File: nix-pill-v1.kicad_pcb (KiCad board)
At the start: 2 copper layers, 75 x 35 mm, 40 parts, among them J1 LEFT, J2 BOOT, J3 RIGHT, J4 SWD, J5 USB_B_Micro, SW1 USER0, SW2 NRST, U1 AMS1117-3.3, U2 STM32F103C8Tx, Y1 32.768KHz LSE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

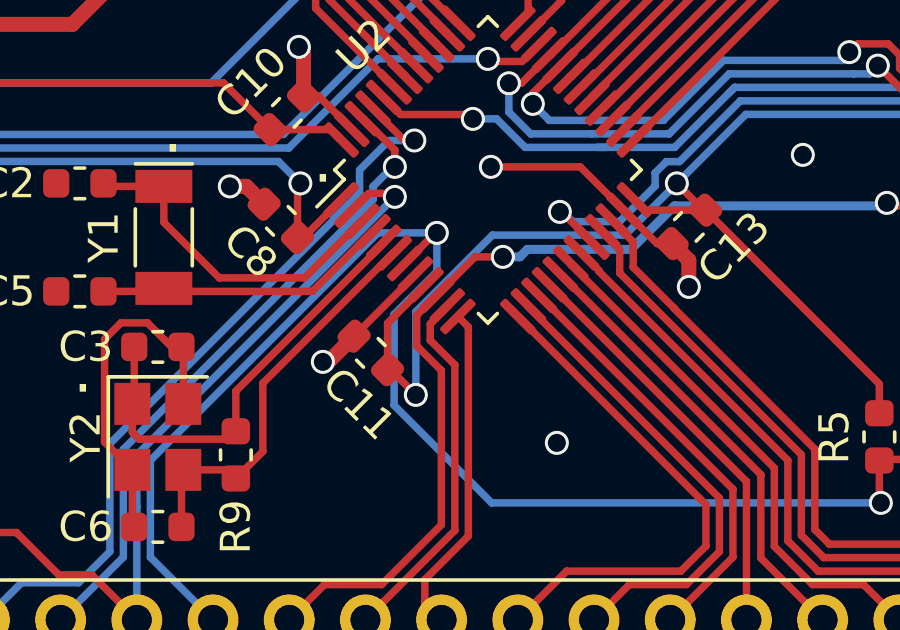
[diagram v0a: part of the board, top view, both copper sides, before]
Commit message: Started adding data sheets Started the BOM Calculated the LED limiting R
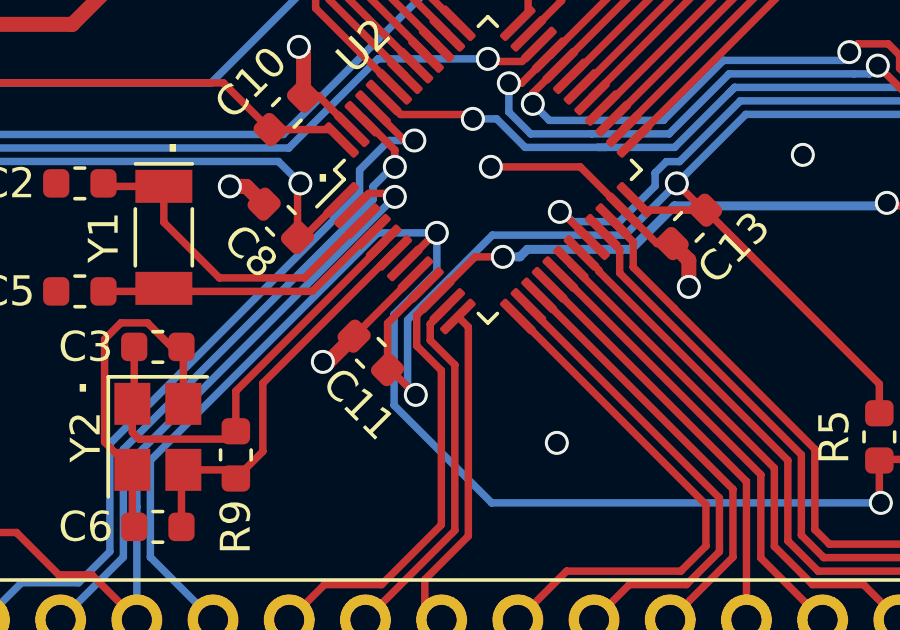
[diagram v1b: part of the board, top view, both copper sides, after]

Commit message: BOM completed. Ordering PCB and parts
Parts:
- C2, C5: value 20pF -> 8pF
- C3, C6: value 20pF -> 10pF
- R1, R2: value 510 -> 100
- R9: value 10M -> 1M
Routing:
- net +3V3: track 214.8 -> 219.5 mm
- net SWDCLK: track 34.5 -> 37.6 mm
- net GND: vias 14 -> 16
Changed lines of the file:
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@@
     (thickness 1.6)
     (drawings 50)
-    (tracks 514)
+    (tracks 522)
     (zones 0)
     (modules 40)
@@
   (page A4)
   (layers
-    (0 F.Cu signal hide)
+    (0 F.Cu signal)
     (31 B.Cu signal)
     (32 B.Adhes user)
@@
       (effects (font (size 1 1) (thickness 0.15)))
     )
-    (fp_text value 20pF (at 0 1.43) (layer F.Fab)
+    (fp_text value 8pF (at 0 1.43) (layer F.Fab)
       (effects (font (size 1 1) (thickness 0.15)))
     )
@@
       (effects (font (size 1 1) (thickness 0.15)))
     )
-    (fp_text value 20pF (at 0 1.43) (layer F.Fab)
+    (fp_text value 10pF (at 0 1.43) (layer F.Fab)
       (effects (font (size 1 1) (thickness 0.15)))
     )
@@
       (effects (font (size 1 1) (thickness 0.15)))
     )
-    (fp_text value 20pF (at 0 1.43) (layer F.Fab)
+    (fp_text value 8pF (at 0 1.43) (layer F.Fab)
       (effects (font (size 1 1) (thickness 0.15)))
     )
@@
       (effects (font (size 1 1) (thickness 0.15)))
     )
-    (fp_text value 20pF (at 0 1.43) (layer F.Fab)
+    (fp_text value 10pF (at 0 1.43) (layer F.Fab)
       (effects (font (size 1 1) (thickness 0.15)))
     )
@@
       (effects (font (size 1 1) (thickness 0.15)))
     )
-    (fp_text value 510 (at 0 1.43 90) (layer F.Fab)
+    (fp_text value 100 (at 0 1.43 90) (layer F.Fab)
       (effects (font (size 1 1) (thickness 0.15)))
     )
@@
       (effects (font (size 1 1) (thickness 0.15)))
     )
-    (fp_text value 510 (at 0 1.43) (layer F.Fab)
+    (fp_text value 100 (at 0 1.43) (layer F.Fab)
       (effects (font (size 1 1) (thickness 0.15)))
     )
@@
       (effects (font (size 1 1) (thickness 0.15)))
     )
-    (fp_text value 10M (at 0 1.43 90) (layer F.Fab)
+    (fp_text value 1M (at 0 1.43 90) (layer F.Fab)
       (effects (font (size 1 1) (thickness 0.15)))
     )
@@
   (segment (start 114.3875 114.6) (end 113.9875 115) (width 0.25) (layer F.Cu) (net 1))
   (segment (start 117.8 114.6) (end 114.3875 114.6) (width 0.25) (layer F.Cu) (net 1))
-  (segment (start 119.3 104.06) (end 120.86 102.5) (width 0.25) (layer F.Cu) (net 1))
-  (segment (start 119.3 106.35) (end 119.3 104.06) (width 0.25) (layer F.Cu) (net 1))
   (segment (start 128.686306 114.6) (end 130.243153 116.156847) (width 0.25) (layer F.Cu) (net 1))
   (segment (start 120.8 114.6) (end 128.686306 114.6) (width 0.25) (layer F.Cu) (net 1))
@@
   (segment (start 146.1 115.65) (end 157.7 115.65) (width 0.25) (layer B.Cu) (net 1))
   (segment (start 114.45 129.5) (end 114.4 129.5) (width 0.25) (layer F.Cu) (net 1))
-  (segment (start 114.4 129.5) (end 113.3 128.4) (width 0.25) (layer F.Cu) (net 1))
-  (segment (start 112.964998 128.4) (end 108.764998 124.2) (width 0.25) (layer F.Cu) (net 1))
-  (segment (start 108.764998 124.2) (end 104.9875 124.2) (width 0.25) (layer F.Cu) (net 1))
-  (segment (start 113.3 128.4) (end 112.964998 128.4) (width 0.25) (layer F.Cu) (net 1))
   (segment (start 134.825009 124.725009) (end 135.1 125) (width 0.25) (layer B.Cu) (net 1))
   (segment (start 134.825009 122.501989) (end 134.825009 124.725009) (width 0.25) (layer B.Cu) (net 1))
@@
   (segment (start 143.8 117.95) (end 142.075001 119.674999) (width 0.25) (layer B.Cu) (net 1))
   (segment (start 142.075001 119.674999) (end 137.651999 119.674999) (width 0.25) (layer B.Cu) (net 1))
+  (segment (start 114.45 129.5) (end 114.45 128.25) (width 0.25) (layer F.Cu) (net 1))
+  (segment (start 114.45 128.25) (end 115.5 127.2) (width 0.25) (layer F.Cu) (net 1))
+  (segment (start 115.5 127.2) (end 115.5 120.7) (width 0.25) (layer F.Cu) (net 1))
+  (segment (start 117.8 118.4) (end 117.8 114.6) (width 0.25) (layer F.Cu) (net 1))
+  (segment (start 115.5 120.7) (end 117.8 118.4) (width 0.25) (layer F.Cu) (net 1))
+  (segment (start 119.3 104.06) (end 120.86 102.5) (width 0.5) (layer F.Cu) (net 1))
+  (segment (start 119.3 106.35) (end 119.3 104.06) (width 0.5) (layer F.Cu) (net 1))
   (via (at 131.2 113.4) (size 0.8) (drill 0.6) (layers F.Cu B.Cu) (net 2))
   (via (at 124 105.6) (size 0.8) (drill 0.6) (layers F.Cu B.Cu) (net 2))
@@
   (via (at 117.4 121.2) (size 0.8) (drill 0.6) (layers F.Cu B.Cu) (net 2))
   (via (at 148 117) (size 0.8) (drill 0.6) (layers F.Cu B.Cu) (net 2))
+  (via (at 111 123.2) (size 0.8) (drill 0.6) (layers F.Cu B.Cu) (net 2))
+  (via (at 166 123.2) (size 0.8) (drill 0.6) (layers F.Cu B.Cu) (net 2))
   (segment (start 124.7875 118.05) (end 124.6875 117.95) (width 0.25) (layer F.Cu) (net 3))
   (segment (start 126.7 118.05) (end 124.7875 118.05) (width 0.25) (layer F.Cu) (net 3))
@@
   (segment (start 139.205895 113.319231) (end 138.637947 113.887179) (width 0.25) (layer F.Cu) (net 45))
   (segment (start 138.637947 113.887179) (end 137.587179 113.887179) (width 0.25) (layer F.Cu) (net 45))
-  (segment (start 106.88999 116.77001) (end 104.8 118.86) (width 0.25) (layer B.Cu) (net 45))
-  (segment (start 137.5 113.8) (end 133.83641 113.8) (width 0.25) (layer B.Cu) (net 45))
-  (segment (start 130.866401 116.770009) (end 106.88999 116.77001) (width 0.25) (layer B.Cu) (net 45))
-  (segment (start 133.83641 113.8) (end 130.866401 116.770009) (width 0.25) (layer B.Cu) (net 45))
-  (segment (start 104.8 116.32) (end 130.68 116.32) (width 0.25) (layer B.Cu) (net 46))
+  (segment (start 136.381637 114.918363) (end 137.5 113.8) (width 0.25) (layer B.Cu) (net 45))
+  (segment (start 135.172222 114.918363) (end 136.381637 114.918363) (width 0.25) (layer B.Cu) (net 45))
+  (segment (start 133.320576 116.770009) (end 135.172222 114.918363) (width 0.25) (layer B.Cu) (net 45))
+  (segment (start 106.88999 116.77001) (end 133.320576 116.770009) (width 0.25) (layer B.Cu) (net 45))
+  (segment (start 104.8 118.86) (end 106.88999 116.77001) (width 0.25) (layer B.Cu) (net 45))
   (segment (start 136.501212 112.612124) (end 136.465856 112.612124) (width 0.25) (layer F.Cu) (net 46))
   (via (at 135.621314 111.378686) (size 0.8) (drill 0.6) (layers F.Cu B.Cu) (net 46))
   (segment (start 136.465856 112.612124) (end 135.621314 111.767582) (width 0.25) (layer F.Cu) (net 46))
   (segment (start 135.621314 111.767582) (end 135.621314 111.378686) (width 0.25) (layer F.Cu) (net 46))
-  (segment (start 135.621314 111.378686) (end 130.68 116.32) (width 0.25) (layer B.Cu) (net 46))
+  (segment (start 133.134175 116.32) (end 134.985822 114.468353) (width 0.25) (layer B.Cu) (net 46))
+  (segment (start 104.8 116.32) (end 133.134175 116.32) (width 0.25) (layer B.Cu) (net 46))
+  (segment (start 136.774999 112.532371) (end 135.621314 111.378686) (width 0.25) (layer B.Cu) (net 46))
+  (segment (start 134.985822 114.468353) (end 136.195237 114.468353) (width 0.25) (layer B.Cu) (net 46))
+  (segment (start 136.195237 114.468353) (end 136.774999 113.888591) (width 0.25) (layer B.Cu) (net 46))
+  (segment (start 136.774999 113.888591) (end 136.774999 112.532371) (width 0.25) (layer B.Cu) (net 46))
   (segment (start 167.8125 118.075) (end 170.235 118.075) (width 0.25) (layer F.Cu) (net 47))
   (segment (start 167.3875 118.5) (end 167.8125 118.075) (width 0.25) (layer F.Cu) (net 47))
